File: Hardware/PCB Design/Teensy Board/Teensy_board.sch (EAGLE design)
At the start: 40 parts, among them IC1 MC7805BDTRKG, IC2 UA78M33CKVU, Q1 PROGRAM_FET, U1 PCA9685PW, U2 74HC4051PW,118, U3 74HC4051PW,118, X1 RJ45-8X, X2 RJ45-8X, X3 RJ45-8X, X4 RJ45-8X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

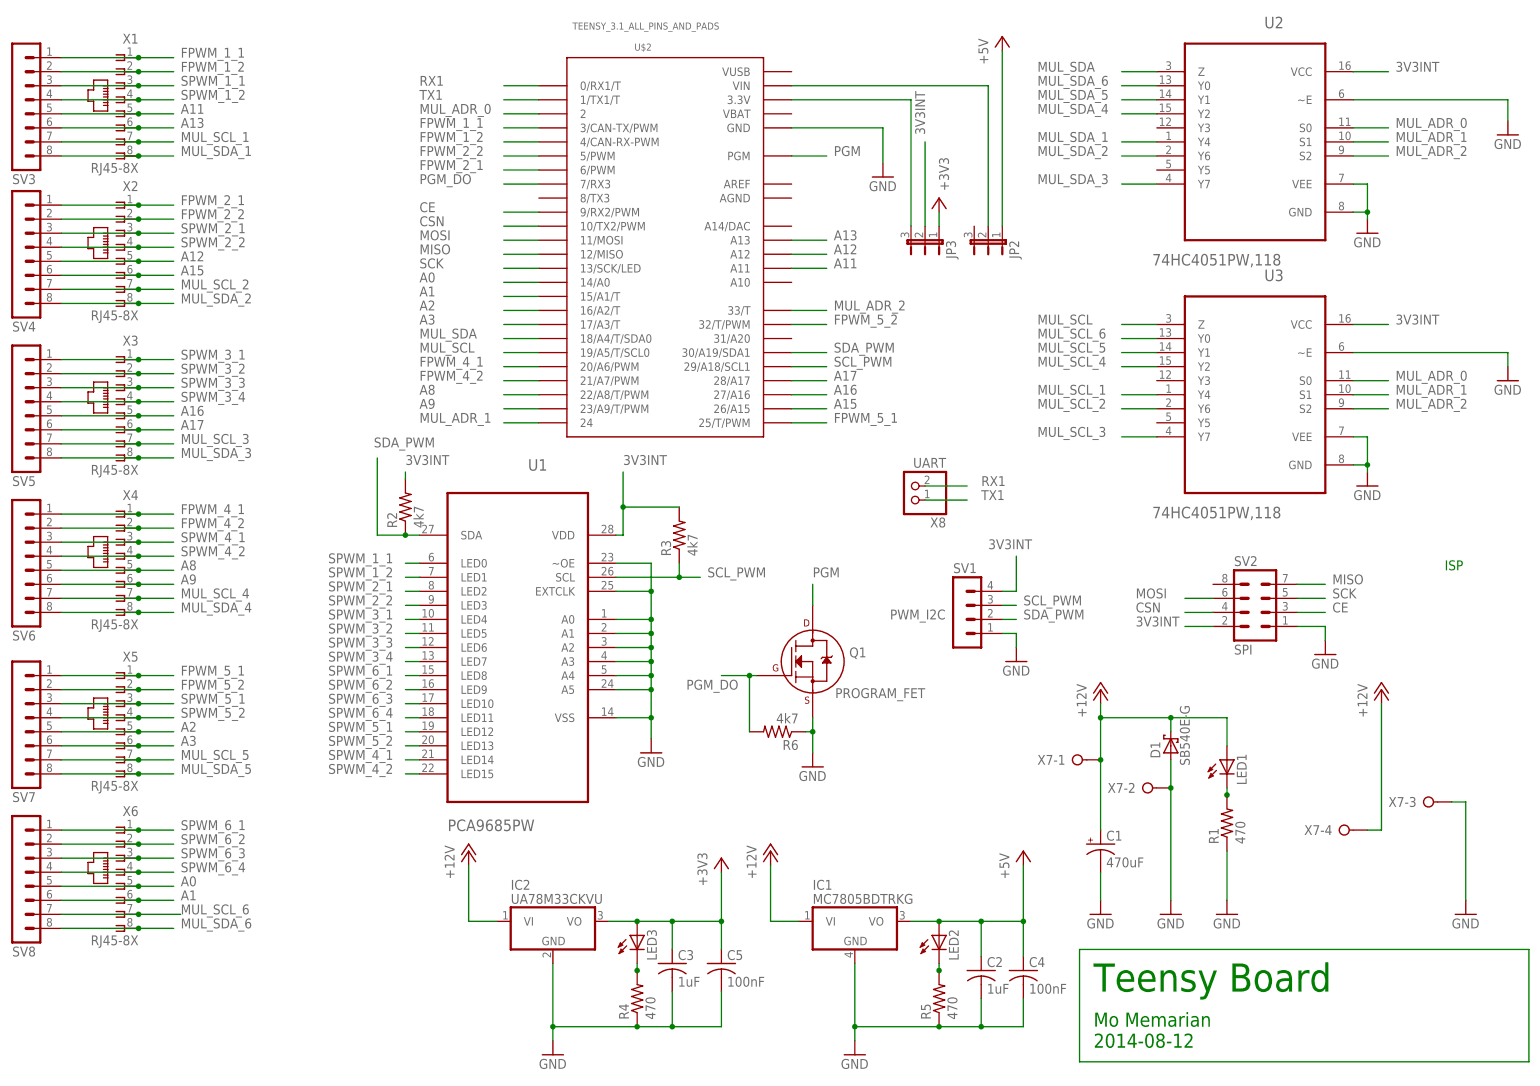
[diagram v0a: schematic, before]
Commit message: Added 4 more power ports; added pull up resistor; made a power plate for the power
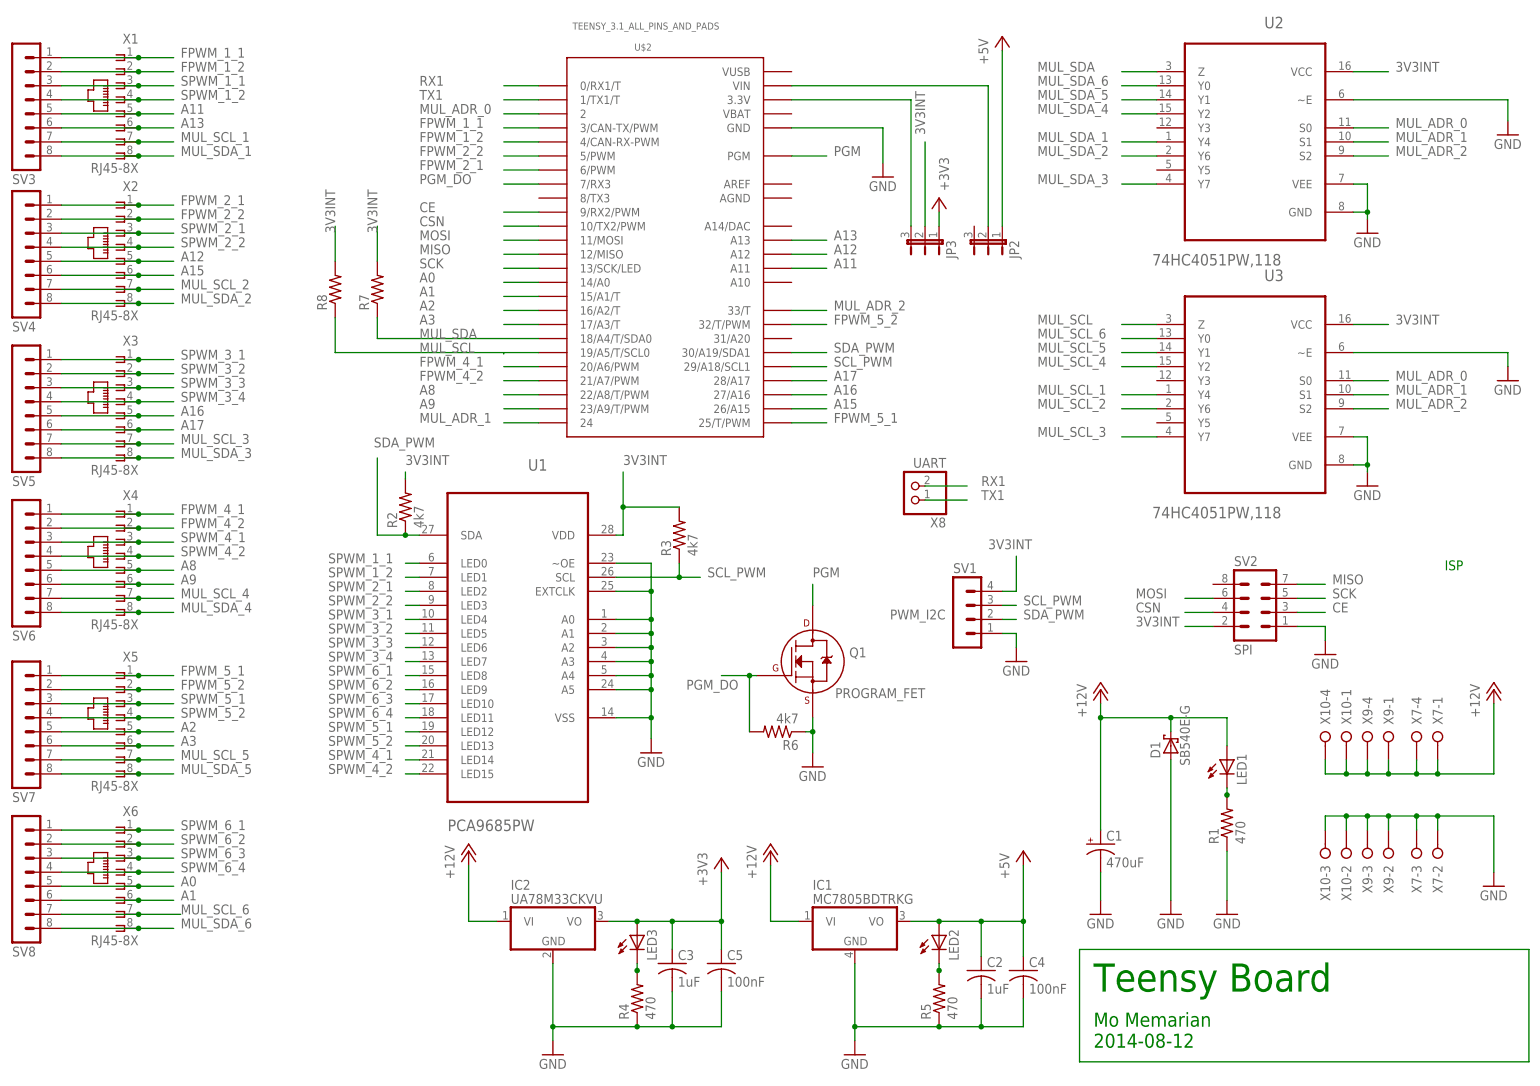
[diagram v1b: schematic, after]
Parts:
- added R7, R8: (no value), CBLA_Test_bed_Library:R-US_R0603
- added X10, X9: (no value), con-wago-508:W237-04P
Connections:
- net +12V: now also X10-1.KL, X10-4.KL, X9-1.KL, X9-4.KL
- net 3V3INT: now also R7.2, R8.2
- net GND: now also X10-2.KL, X10-3.KL, X9-2.KL, X9-3.KL
- net MUL_SCL: now also R8.1
- net MUL_SDA: now also R7.1
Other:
- moved on the sheet: X7-1, X7-2, X7-3, X7-4
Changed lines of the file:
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@@
 <setting verticaltext="up"/>
 </settings>
-<grid distance="0.1" unitdist="inch" unit="inch" style="lines" multiple="1" display="no" altdistance="0.01" altunitdist="inch" altunit="inch"/>
+<grid distance="0.05" unitdist="inch" unit="inch" style="lines" multiple="1" display="no" altdistance="0.01" altunitdist="inch" altunit="inch"/>
 <layers>
 <layer number="1" name="Top" color="4" fill="1" visible="no" active="no"/>
@@
 <part name="D1" library="CBLA_Test_bed_Library" deviceset="SB540E-G" device=""/>
 <part name="LED1" library="led" deviceset="LED" device="SML1206"/>
-<part name="X7" library="con-wago-508" deviceset="W237-04P" device=""/>
 <part name="PE3" library="supply1" deviceset="GND" device=""/>
 <part name="R1" library="CBLA_Test_bed_Library" deviceset="R-US_" device="R0603" value="470"/>
@@
 <part name="SV8" library="con-lstb" deviceset="MA08-1" device=""/>
 <part name="X8" library="CBLA_Test_bed_Library" deviceset="PINHD-1X2" device="" value="UART"/>
+<part name="R7" library="CBLA_Test_bed_Library" deviceset="R-US_" device="R0603"/>
+<part name="R8" library="CBLA_Test_bed_Library" deviceset="R-US_" device="R0603"/>
+<part name="X7" library="con-wago-508" deviceset="W237-04P" device=""/>
+<part name="X9" library="con-wago-508" deviceset="W237-04P" device=""/>
+<part name="X10" library="con-wago-508" deviceset="W237-04P" device=""/>
 </parts>
 <sheets>
@@
 <instance part="PE18" gate="1" x="232.41" y="34.29"/>
 <instance part="PE19" gate="1" x="209.55" y="34.29"/>
-<instance part="PE20" gate="1" x="275.59" y="34.29"/>
-<instance part="P+14" gate="1" x="260.35" y="74.93"/>
+<instance part="PE20" gate="1" x="280.67" y="39.37"/>
+<instance part="P+14" gate="1" x="280.67" y="74.93"/>
 <instance part="D1" gate="G$1" x="222.25" y="64.77" smashed="yes" rot="R90">
 <attribute name="NAME" x="220.345" y="62.484" size="1.778" layer="95" rot="R90"/>
@@
 </instance>
 <instance part="LED1" gate="G$1" x="232.41" y="62.23"/>
-<instance part="X7" gate="-1" x="204.47" y="62.23"/>
-<instance part="X7" gate="-2" x="217.17" y="57.15"/>
-<instance part="X7" gate="-3" x="267.97" y="54.61"/>
-<instance part="X7" gate="-4" x="252.73" y="49.53"/>
 <instance part="PE3" gate="1" x="222.25" y="34.29"/>
 <instance part="R1" gate="G$1" x="232.41" y="50.8" rot="R90"/>
@@
 <instance part="SV8" gate="1" x="13.97" y="41.91" rot="MR180"/>
 <instance part="X8" gate="G$1" x="175.26" y="111.76" rot="R180"/>
+<instance part="R7" gate="G$1" x="78.74" y="147.32" rot="R90"/>
+<instance part="R8" gate="G$1" x="71.12" y="147.32" rot="R90"/>
+<instance part="X7" gate="-1" x="270.51" y="67.31" rot="R270"/>
+<instance part="X7" gate="-2" x="270.51" y="44.45" rot="R90"/>
+<instance part="X7" gate="-3" x="266.7" y="44.45" rot="R90"/>
+<instance part="X7" gate="-4" x="266.7" y="67.31" rot="R270"/>
+<instance part="X9" gate="-1" x="261.62" y="67.31" rot="R270"/>
+<instance part="X9" gate="-2" x="261.62" y="44.45" rot="R90"/>
+<instance part="X9" gate="-3" x="257.81" y="44.45" rot="R90"/>
+<instance part="X9" gate="-4" x="257.81" y="67.31" rot="R270"/>
+<instance part="X10" gate="-1" x="254" y="67.31" rot="R270"/>
+<instance part="X10" gate="-2" x="254" y="44.45" rot="R90"/>
+<instance part="X10" gate="-3" x="250.19" y="44.45" rot="R90"/>
+<instance part="X10" gate="-4" x="250.19" y="67.31" rot="R270"/>
 </instances>
 <busses>
@@
 <pinref part="P+3" gate="1" pin="+12V"/>
 <wire x1="209.55" y1="72.39" x2="209.55" y2="69.85" width="0.1524" layer="91"/>
-<wire x1="209.55" y1="69.85" x2="209.55" y2="62.23" width="0.1524" layer="91"/>
-<wire x1="209.55" y1="62.23" x2="209.55" y2="49.53" width="0.1524" layer="91"/>
+<wire x1="209.55" y1="69.85" x2="209.55" y2="49.53" width="0.1524" layer="91"/>
 <wire x1="209.55" y1="69.85" x2="222.25" y2="69.85" width="0.1524" layer="91"/>
 <junction x="209.55" y="69.85"/>
@@
 <wire x1="222.25" y1="69.85" x2="232.41" y2="69.85" width="0.1524" layer="91"/>
 <junction x="222.25" y="69.85"/>
-<pinref part="X7" gate="-1" pin="KL"/>
-<junction x="209.55" y="62.23"/>
 <pinref part="LED1" gate="G$1" pin="A"/>
 <wire x1="232.41" y1="69.85" x2="232.41" y2="64.77" width="0.1524" layer="91"/>
 </segment>
 <segment>
-<wire x1="260.35" y1="72.39" x2="260.35" y2="49.53" width="0.1524" layer="91"/>
+<wire x1="280.67" y1="72.39" x2="280.67" y2="59.69" width="0.1524" layer="91"/>
 <pinref part="P+14" gate="1" pin="+12V"/>
-<wire x1="260.35" y1="49.53" x2="257.81" y2="49.53" width="0.1524" layer="91"/>
+<pinref part="X10" gate="-4" pin="KL"/>
+<wire x1="280.67" y1="59.69" x2="270.51" y2="59.69" width="0.1524" layer="91"/>
+<wire x1="270.51" y1="59.69" x2="266.7" y2="59.69" width="0.1524" layer="91"/>
+<wire x1="266.7" y1="59.69" x2="261.62" y2="59.69" width="0.1524" layer="91"/>
+<wire x1="261.62" y1="59.69" x2="257.81" y2="59.69" width="0.1524" layer="91"/>
+<wire x1="257.81" y1="59.69" x2="254" y2="59.69" width="0.1524" layer="91"/>
+<wire x1="254" y1="59.69" x2="250.19" y2="59.69" width="0.1524" layer="91"/>
+<wire x1="250.19" y1="59.69" x2="250.19" y2="62.23" width="0.1524" layer="91"/>
+<pinref part="X10" gate="-1" pin="KL"/>
+<wire x1="254" y1="59.69" x2="254" y2="62.23" width="0.1524" layer="91"/>
+<junction x="254" y="59.69"/>
+<pinref part="X9" gate="-4" pin="KL"/>
+<wire x1="257.81" y1="59.69" x2="257.81" y2="62.23" width="0.1524" layer="91"/>
+<junction x="257.81" y="59.69"/>
+<pinref part="X9" gate="-1" pin="KL"/>
+<wire x1="261.62" y1="59.69" x2="261.62" y2="62.23" width="0.1524" layer="91"/>
+<junction x="261.62" y="59.69"/>
 <pinref part="X7" gate="-4" pin="KL"/>
+<wire x1="266.7" y1="59.69" x2="266.7" y2="62.23" width="0.1524" layer="91"/>
+<junction x="266.7" y="59.69"/>
+<pinref part="X7" gate="-1" pin="KL"/>
+<wire x1="270.51" y1="59.69" x2="270.51" y2="62.23" width="0.1524" layer="91"/>
+<junction x="270.51" y="59.69"/>
 </segment>
 <segment>
@@
 </segment>
 <segment>
-<pinref part="PE20" gate="1" pin="GND"/>
-<wire x1="275.59" y1="54.61" x2="275.59" y2="36.83" width="0.1524" layer="91"/>
-<wire x1="273.05" y1="54.61" x2="275.59" y2="54.61" width="0.1524" layer="91"/>
-<pinref part="X7" gate="-3" pin="KL"/>
-</segment>
-<segment>
 <pinref part="D1" gate="G$1" pin="A"/>
-<wire x1="222.25" y1="62.23" x2="222.25" y2="57.15" width="0.1524" layer="91"/>
-<pinref part="X7" gate="-2" pin="KL"/>
-<junction x="222.25" y="57.15"/>
 <pinref part="PE3" gate="1" pin="GND"/>
-<wire x1="222.25" y1="57.15" x2="222.25" y2="36.83" width="0.1524" layer="91"/>
+<wire x1="222.25" y1="62.23" x2="222.25" y2="36.83" width="0.1524" layer="91"/>
 </segment>
 <segment>
@@
 <pinref part="PE18" gate="1" pin="GND"/>
 </segment>
+<segment>
+<pinref part="X10" gate="-3" pin="KL"/>
+<wire x1="250.19" y1="49.53" x2="250.19" y2="52.07" width="0.1524" layer="91"/>
+<pinref part="PE20" gate="1" pin="GND"/>
+<wire x1="250.19" y1="52.07" x2="254" y2="52.07" width="0.1524" layer="91"/>
+<wire x1="254" y1="52.07" x2="257.81" y2="52.07" width="0.1524" layer="91"/>
+<wire x1="257.81" y1="52.07" x2="261.62" y2="52.07" width="0.1524" layer="91"/>
+<wire x1="261.62" y1="52.07" x2="266.7" y2="52.07" width="0.1524" layer="91"/>
+<wire x1="266.7" y1="52.07" x2="270.51" y2="52.07" width="0.1524" layer="91"/>
+<wire x1="270.51" y1="52.07" x2="280.67" y2="52.07" width="0.1524" layer="91"/>
+<wire x1="280.67" y1="52.07" x2="280.67" y2="41.91" width="0.1524" layer="91"/>
+<wire x1="254" y1="52.07" x2="254" y2="49.53" width="0.1524" layer="91"/>
+<junction x="254" y="52.07"/>
+<pinref part="X9" gate="-3" pin="KL"/>
+<wire x1="257.81" y1="52.07" x2="257.81" y2="49.53" width="0.1524" layer="91"/>
+<junction x="257.81" y="52.07"/>
+<wire x1="261.62" y1="52.07" x2="261.62" y2="49.53" width="0.1524" layer="91"/>
+<junction x="261.62" y="52.07"/>
+<wire x1="266.7" y1="52.07" x2="266.7" y2="49.53" width="0.1524" layer="91"/>
+<junction x="266.7" y="52.07"/>
+<wire x1="270.51" y1="52.07" x2="270.51" y2="49.53" width="0.1524" layer="91"/>
+<junction x="270.51" y="52.07"/>
+<pinref part="X10" gate="-2" pin="KL"/>
+<pinref part="X9" gate="-2" pin="KL"/>
+<pinref part="X7" gate="-3" pin="KL"/>
+<pinref part="X7" gate="-2" pin="KL"/>
+</segment>
 </net>
 <net name="+3V3" class="0">
@@
 <segment>
 <pinref part="U$2" gate="G$1" pin="19/A5/T/SCL0"/>
-<wire x1="107.95" y1="135.89" x2="101.6" y2="135.89" width="0.1524" layer="91"/>
 <label x="86.36" y="135.89" size="1.778" layer="95"/>
+<wire x1="71.12" y1="135.89" x2="107.95" y2="135.89" width="0.1524" layer="91"/>
+<pinref part="R8" gate="G$1" pin="1"/>
+<wire x1="71.12" y1="142.24" x2="71.12" y2="135.89" width="0.1524" layer="91"/>
 </segment>
 <segment>
@@
 <segment>
 <pinref part="U$2" gate="G$1" pin="18/A4/T/SDA0"/>
-<wire x1="107.95" y1="138.43" x2="101.6" y2="138.43" width="0.1524" layer="91"/>
 <label x="86.36" y="138.43" size="1.778" layer="95"/>
+<pinref part="R7" gate="G$1" pin="1"/>
+<wire x1="78.74" y1="142.24" x2="78.74" y2="138.43" width="0.1524" layer="91"/>
+<wire x1="78.74" y1="138.43" x2="107.95" y2="138.43" width="0.1524" layer="91"/>
 </segment>
 <segment>
@@
 <wire x1="224.79" y1="86.36" x2="229.87" y2="86.36" width="0.1524" layer="91"/>
 </segment>
+<segment>
+<wire x1="71.12" y1="158.75" x2="71.12" y2="152.4" width="0.1524" layer="91"/>
+<label x="71.12" y="157.48" size="1.778" layer="95" rot="R90"/>
+<label x="78.74" y="157.48" size="1.778" layer="95" rot="R90"/>
+<pinref part="R8" gate="G$1" pin="2"/>
+</segment>
+<segment>
+<wire x1="78.74" y1="158.75" x2="78.74" y2="152.4" width="0.1524" layer="91"/>
+<pinref part="R7" gate="G$1" pin="2"/>
+</segment>
 </net>
 <net name="TEENSY_VIN" class="0">
@@
 </segment>
 </net>
+<net name="N$1" class="0">
+<segment>
+<wire x1="101.6" y1="135.89" x2="101.6" y2="135.636" width="0.1524" layer="91"/>
+</segment>
+</net>

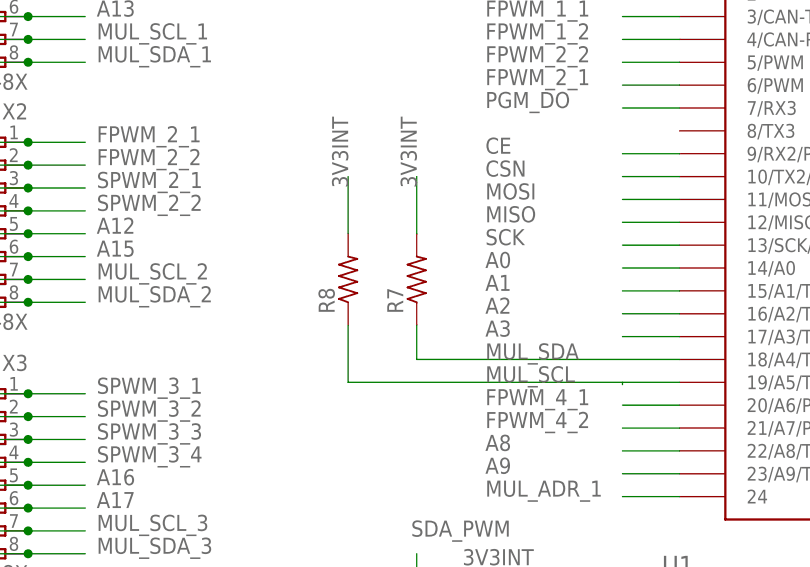
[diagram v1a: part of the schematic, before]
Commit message: Added resistor value to the i2c pull up
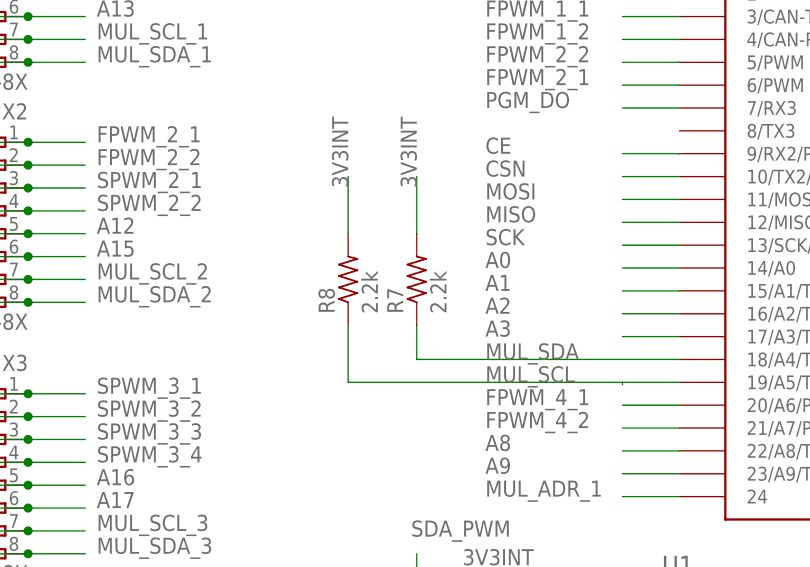
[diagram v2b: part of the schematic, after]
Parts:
- R7, R8: value (none) -> 2.2k
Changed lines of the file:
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@@
 <setting verticaltext="up"/>
 </settings>
-<grid distance="0.05" unitdist="inch" unit="inch" style="lines" multiple="1" display="no" altdistance="0.01" altunitdist="inch" altunit="inch"/>
+<grid distance="0.1" unitdist="inch" unit="inch" style="lines" multiple="1" display="no" altdistance="0.01" altunitdist="inch" altunit="inch"/>
 <layers>
 <layer number="1" name="Top" color="4" fill="1" visible="no" active="no"/>
@@
 <part name="SV8" library="con-lstb" deviceset="MA08-1" device=""/>
 <part name="X8" library="CBLA_Test_bed_Library" deviceset="PINHD-1X2" device="" value="UART"/>
-<part name="R7" library="CBLA_Test_bed_Library" deviceset="R-US_" device="R0603"/>
-<part name="R8" library="CBLA_Test_bed_Library" deviceset="R-US_" device="R0603"/>
+<part name="R7" library="CBLA_Test_bed_Library" deviceset="R-US_" device="R0603" value="2.2k"/>
+<part name="R8" library="CBLA_Test_bed_Library" deviceset="R-US_" device="R0603" value="2.2k"/>
 <part name="X7" library="con-wago-508" deviceset="W237-04P" device=""/>
 <part name="X9" library="con-wago-508" deviceset="W237-04P" device=""/>

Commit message: Made Teensy Board smaller by moving the RJ45 connector to another board
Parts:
- removed X1, X2, X3, X4, X5, X6: RJ45-8X, CBLA_Test_bed_Library:RJ45-8X
- removed X10: (no value), con-wago-508:W237-04P
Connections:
- net +12V: no longer X10-1.KL, X10-4.KL
- net A0: no longer X6.5
- net A1: no longer X6.6
- net A11: no longer X1.5
- net A12: no longer X2.5
- net A13: no longer X1.6
- net A15: no longer X2.6
- net A16: no longer X3.5
- net A17: no longer X3.6
- net A2: no longer X5.5
- net A3: no longer X5.6
- net A8: no longer X4.5
- net A9: no longer X4.6
- net FPWM_1_1: no longer X1.1
- net FPWM_1_2: no longer X1.2
- net FPWM_2_1: no longer X2.1
- net FPWM_2_2: no longer X2.2
- net FPWM_4_1: no longer X4.1
- net FPWM_4_2: no longer X4.2
- net FPWM_5_1: no longer X5.1
- net FPWM_5_2: no longer X5.2
- net GND: no longer X10-2.KL, X10-3.KL
- net MUL_SCL_1: no longer X1.7
- net MUL_SCL_2: no longer X2.7
- net MUL_SCL_3: no longer X3.7
- net MUL_SCL_4: no longer X4.7
- net MUL_SCL_5: no longer X5.7
- net MUL_SCL_6: no longer X6.7
- net MUL_SDA_1: no longer X1.8
- net MUL_SDA_2: no longer X2.8
- net MUL_SDA_3: no longer X3.8
- net MUL_SDA_4: no longer X4.8
- net MUL_SDA_5: no longer X5.8
- net MUL_SDA_6: no longer X6.8
- net SPWM_1_1: no longer X1.3
- net SPWM_1_2: no longer X1.4
- net SPWM_2_1: no longer X2.3
- net SPWM_2_2: no longer X2.4
- net SPWM_3_1: no longer X3.1
- net SPWM_3_2: no longer X3.2
- net SPWM_3_3: no longer X3.3
- net SPWM_3_4: no longer X3.4
- net SPWM_4_1: no longer X4.3
- net SPWM_4_2: no longer X4.4
- net SPWM_5_1: no longer X5.3
- net SPWM_5_2: no longer X5.4
- net SPWM_6_1: no longer X6.1
- net SPWM_6_2: no longer X6.2
- net SPWM_6_3: no longer X6.3
- net SPWM_6_4: no longer X6.4
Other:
- note added: "Mo Memarian & Matthew Chan 2014-10-16"
- note removed: "Mo Memarian 2014-08-12"
